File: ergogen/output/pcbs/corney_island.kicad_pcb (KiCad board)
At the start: 2 copper layers, 117.7 x 96.7 mm, 89 parts

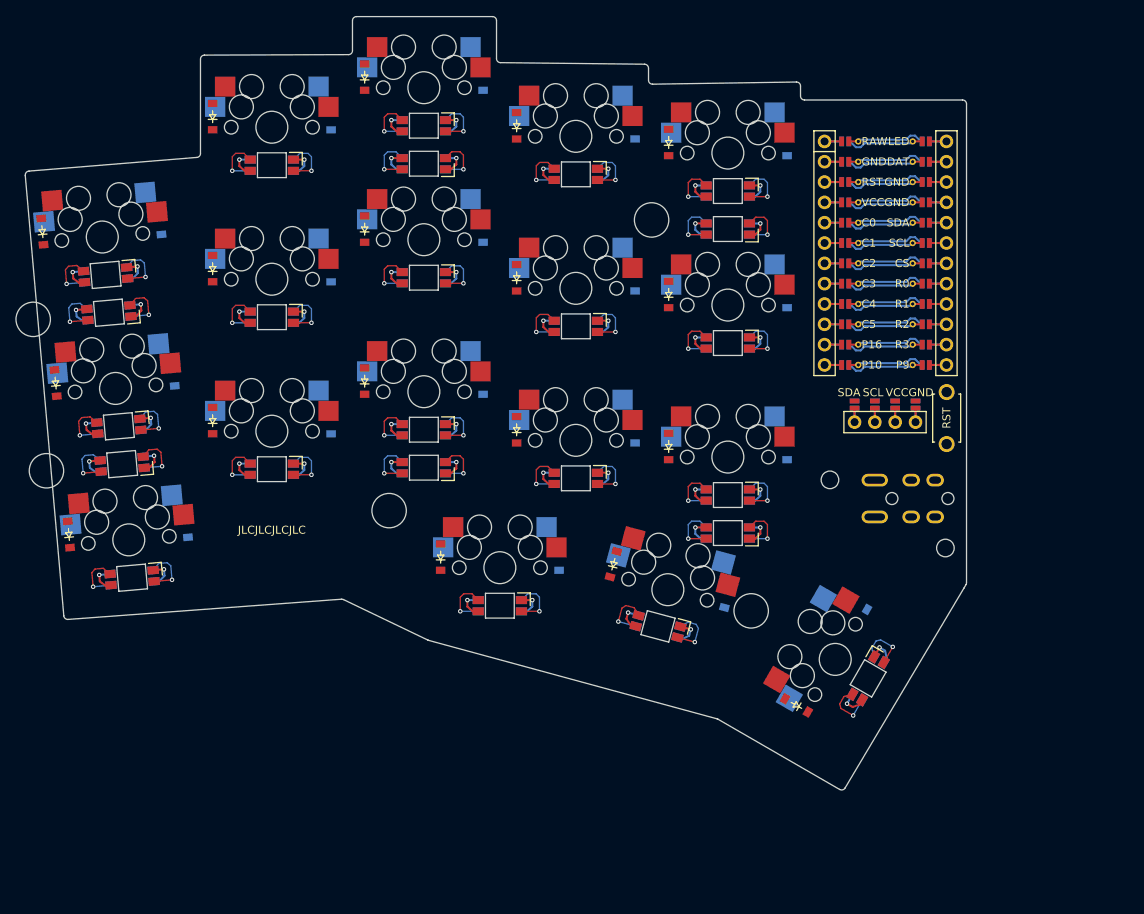
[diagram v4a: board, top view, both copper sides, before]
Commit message: Changed thumb splay
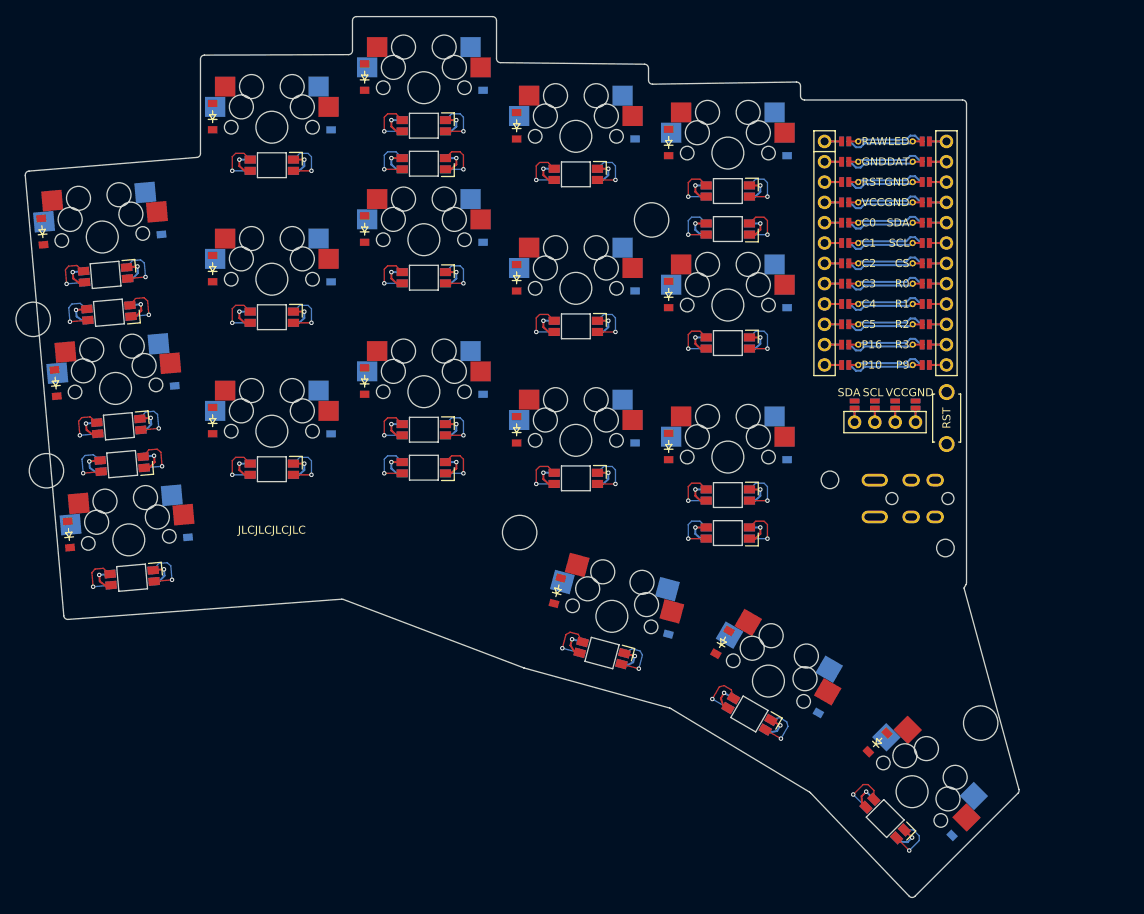
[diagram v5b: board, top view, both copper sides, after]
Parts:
- moved MH7 31.9 mm to (206.5, 122.9), turned to -45 degrees
- moved D18 30.9 mm to (204.1, 135.8), turned to 45 degrees
- moved S18 19.1 mm to (197.9, 131.5), turned to -45 degrees
- moved D17 18.0 mm to (187.0, 120.2), turned to 60 degrees
- moved LED18 17.7 mm to (194.6, 134.8), turned to 135 degrees
- moved S17 17.0 mm to (180.0, 117.7), turned to -30 degrees
- moved D35 16.8 mm to (174.2, 112.8), turned to 60 degrees
- moved MH6 16.5 mm to (148.9, 99.1), turned to -15 degrees
- moved D16 16.2 mm to (167.9, 110.2), turned to 75 degrees
- moved LED17 15.8 mm to (177.6, 121.8), turned to 150 degrees
- moved S16 15.3 mm to (160.4, 109.6), turned to -15 degrees
- moved D34 15.2 mm to (153.6, 106.4), turned to 75 degrees
- moved LED16 14.1 mm to (159.2, 114.1), turned to 165 degrees
- moved D36 11.2 mm to (193.6, 125.3), turned to 45 degrees
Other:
- board size 117.7 x 96.7 mm -> 124.2 x 110.1 mm

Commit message: Moved screws back onto board
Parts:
- moved MH3 24.2 mm to (107.4, 57.9), turned to 0 degrees
- moved MH4 23.6 mm to (108.4, 76.9), turned to 0 degrees
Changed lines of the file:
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@@
   )
   (module "ceoloide:mounting_hole_npth" (layer F.Cu)
-      (at 88.05221169999999 72.4364306 5)
-      (fp_text reference "MH3" (at 0 2.55 5) (layer F.SilkS) hide (effects (font (size 1 1) (thickness 0.15))))
-      (pad "" np_thru_hole circle (at 0 0 5) (size 4.3 4.3) (drill 4.3) (layers *.Cu *.Mask))
+      (at 107.384445 57.919590400000004 0)
+      (fp_text reference "MH3" (at 0 2.55 0) (layer F.SilkS) hide (effects (font (size 1 1) (thickness 0.15))))
+      (pad "" np_thru_hole circle (at 0 0 0) (size 4.3 4.3) (drill 4.3) (layers *.Cu *.Mask))
   )
   (module "ceoloide:mounting_hole_npth" (layer F.Cu)
-      (at 89.70817079999999 91.3641299 5)
-      (fp_text reference "MH4" (at 0 2.55 5) (layer F.SilkS) hide (effects (font (size 1 1) (thickness 0.15))))
-      (pad "" np_thru_hole circle (at 0 0 5) (size 4.3 4.3) (drill 4.3) (layers *.Cu *.Mask))
+      (at 108.384445 76.9195904 0)
+      (fp_text reference "MH4" (at 0 2.55 0) (layer F.SilkS) hide (effects (font (size 1 1) (thickness 0.15))))
+      (pad "" np_thru_hole circle (at 0 0 0) (size 4.3 4.3) (drill 4.3) (layers *.Cu *.Mask))
   )
   (module "ceoloide:mounting_hole_npth" (layer F.Cu)

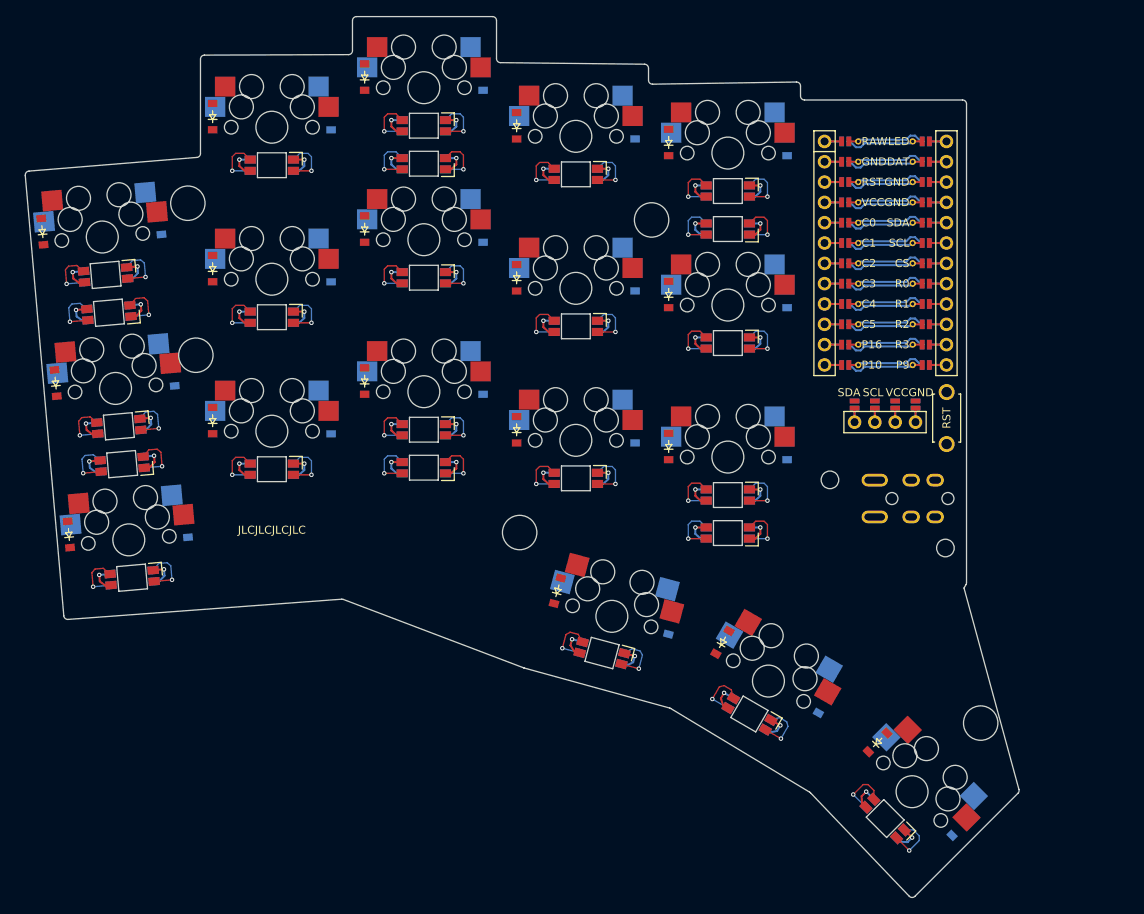
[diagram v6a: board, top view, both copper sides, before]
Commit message: Moved screws around a bit
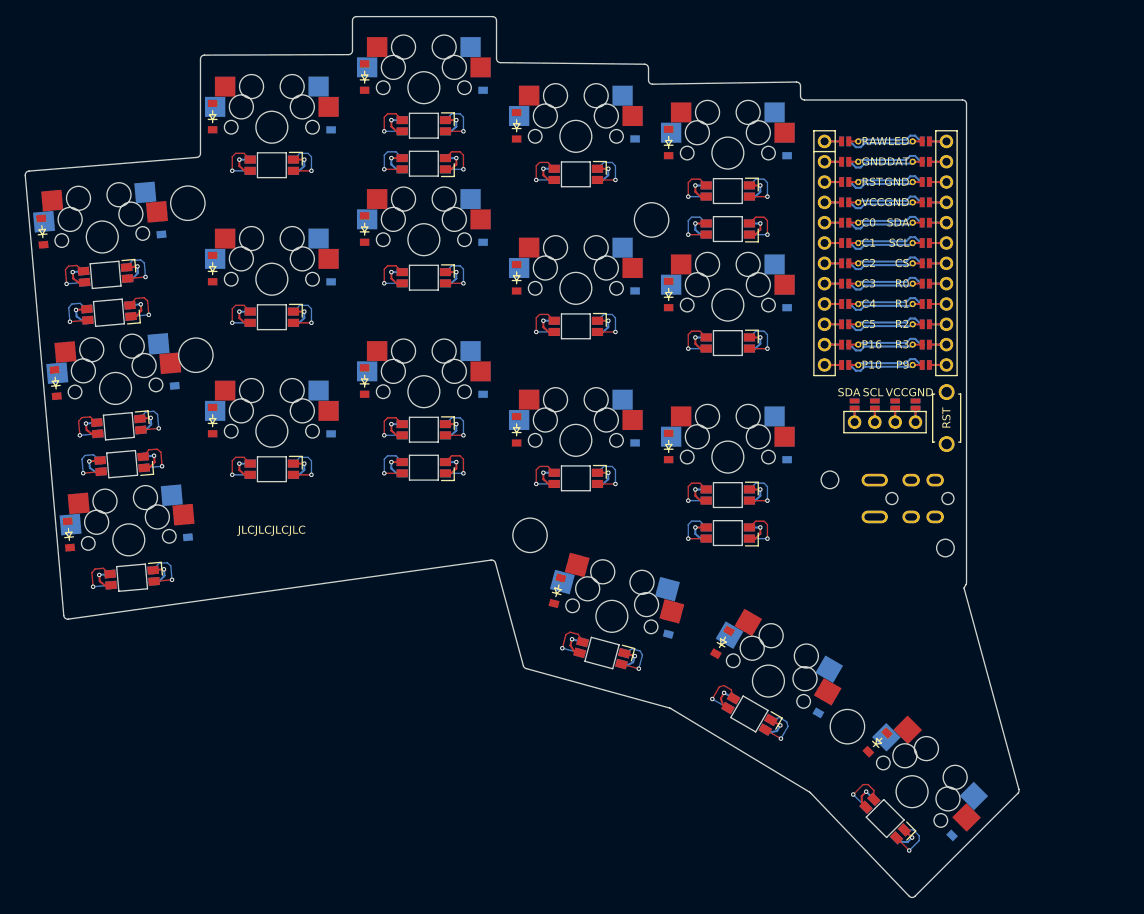
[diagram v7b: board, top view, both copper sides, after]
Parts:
- moved MH7 16.7 mm to (189.8, 123.4), turned to -30 degrees
- moved MH6 1.34 mm to (150.2, 99.4)
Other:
- outline, holes or cut-outs redrawn
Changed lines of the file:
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@@
   )
   (module "ceoloide:mounting_hole_npth" (layer F.Cu)
-      (at 148.8598077 99.0848776 -15)
+      (at 150.1570461 99.4324716 -15)
       (fp_text reference "MH6" (at 0 2.55 -15) (layer F.SilkS) hide (effects (font (size 1 1) (thickness 0.15))))
       (pad "" np_thru_hole circle (at 0 0 -15) (size 4.3 4.3) (drill 4.3) (layers *.Cu *.Mask))
   )
   (module "ceoloide:mounting_hole_npth" (layer F.Cu)
-      (at 206.488576 122.90275019999999 -45)
-      (fp_text reference "MH7" (at 0 2.55 -45) (layer F.SilkS) hide (effects (font (size 1 1) (thickness 0.15))))
-      (pad "" np_thru_hole circle (at 0 0 -45) (size 4.3 4.3) (drill 4.3) (layers *.Cu *.Mask))
+      (at 189.8298246 123.3510864 -30)
+      (fp_text reference "MH7" (at 0 2.55 -30) (layer F.SilkS) hide (effects (font (size 1 1) (thickness 0.15))))
+      (pad "" np_thru_hole circle (at 0 0 -30) (size 4.3 4.3) (drill 4.3) (layers *.Cu *.Mask))
   )
       (module MX (layer F.Cu)
@@
     (segment (start 179.834 98.090) (end 179.834 99.850) (width 0.15) (layer "F.Cu") (net 95))
     (segment (start 179.413 97.665) (end 179.834 98.090) (width 0.15) (layer "F.Cu") (net 95))
-  (gr_line (start 91.87824460323029 109.49068746980254) (end 87.06061104775414 54.447423555018986) (layer Edge.Cuts) (stroke (width 0.15) (type default)))
+  (gr_line (start 91.87535728883249 109.45769882370212) (end 87.06061104775414 54.447423555018986) (layer Edge.Cuts) (stroke (width 0.15) (type default)))
 (gr_line (start 87.51811429808367 53.90547845906503) (end 108.50503754967045 52.19601094528491) (layer Edge.Cuts) (stroke (width 0.15) (type default)))
 (gr_line (start 108.964445 51.69766144933076) (end 108.964445 39.90788282277217) (layer Edge.Cuts) (stroke (width 0.15) (type default)))
@@
 (gr_line (start 197.5573001306715 144.5456552181502) (end 185.2184018103768 131.6245719172887) (layer Edge.Cuts) (stroke (width 0.15) (type default)))
 (gr_line (start 185.11474537091743 131.54156036435938) (end 167.73632242747522 121.07577102297391) (layer Edge.Cuts) (stroke (width 0.15) (type default)))
-(gr_line (start 167.61101352447525 121.02201021014679) (end 149.42297909295323 116.01776895205687) (layer Edge.Cuts) (stroke (width 0.15) (type default)))
-(gr_line (start 149.37827902664569 116.003177061327) (end 126.82809141312292 107.44890800214452) (layer Edge.Cuts) (stroke (width 0.15) (type default)))
-(gr_line (start 126.61389341312291 107.4177619021445) (end 92.41319770323031 109.94573156980263) (layer Edge.Cuts) (stroke (width 0.15) (type default)))
+(gr_line (start 167.61101352447525 121.02201021014679) (end 149.67542832928424 116.0872276331902) (layer Edge.Cuts) (stroke (width 0.15) (type default)))
+(gr_line (start 149.32552987561743 115.73612318902917) (end 145.83984366392013 102.89472334271511) (layer Edge.Cuts) (stroke (width 0.15) (type default)))
+(gr_line (start 145.28816068340882 102.53050838832783) (end 92.4425969819845 109.90929922465821) (layer Edge.Cuts) (stroke (width 0.15) (type default)))
 (gr_line (start 184.46722317371226 45.01459040000001) (end 204.2174451 45.01459040000001) (layer Edge.Cuts) (stroke (width 0.15) (type default)))
 (gr_line (start 204.7174451 45.51459040000001) (end 204.7174451 105.34161580612954) (layer Edge.Cuts) (stroke (width 0.15) (type default)))
@@
 (gr_arc (start 185.21840173422504 131.62457194226215) (mid 185.16934173422504 131.57960944226215) (end 185.11474533422503 131.54156034226216) (layer Edge.Cuts) (stroke (width 0.15) (type default)))
 (gr_arc (start 167.7363223907828 121.07577100087666) (mid 167.6755091907828 121.04459890087666) (end 167.6110134907828 121.02201020087666) (layer Edge.Cuts) (stroke (width 0.15) (type default)))
-(gr_arc (start 149.37827902664569 116.003177061327) (mid 149.4004574266457 116.010998761327) (end 149.42297912664569 116.017768961327) (layer Edge.Cuts) (stroke (width 0.15) (type default)))
-(gr_arc (start 126.8280914131229 107.4489080021445) (mid 126.72269801312291 107.4216051021445) (end 126.61389341312291 107.4177619021445) (layer Edge.Cuts) (stroke (width 0.15) (type default)))
-(gr_arc (start 91.8782446032303 109.49068746980264) (mid 92.0523782032303 109.82794416980263) (end 92.4131977032303 109.94573156980263) (layer Edge.Cuts) (stroke (width 0.15) (type default)))
+(gr_arc (start 149.32552986297674 115.73612314246033) (mid 149.45390776297674 115.95808674246032) (end 149.67542826297674 116.08722764246032) (layer Edge.Cuts) (stroke (width 0.15) (type default)))
+(gr_arc (start 145.83984367656083 102.89472338928387) (mid 145.63278067656083 102.60843598928388) (end 145.28816067656084 102.53050828928387) (layer Edge.Cuts) (stroke (width 0.15) (type default)))
+(gr_arc (start 91.87535728883246 109.45769882370203) (mid 92.06202788883246 109.80527372370203) (end 92.44259698883246 109.90929922370204) (layer Edge.Cuts) (stroke (width 0.15) (type default)))
 )

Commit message: Tweak shape
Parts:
- removed MH6, MH7: , ceoloide:mounting_hole_npth
- moved MH2 96.7 mm to (108.4, 76.9)
- moved MH1 87.4 mm to (107.4, 57.9)
- moved MH5 67.9 mm to (189.8, 123.4), turned to -30 degrees
- moved MH3 58.0 mm to (165.4, 60.0)
- moved MH4 47.5 mm to (150.2, 99.4), turned to -15 degrees
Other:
- board size 124.2 x 110.1 mm -> 124.1 x 110.1 mm
